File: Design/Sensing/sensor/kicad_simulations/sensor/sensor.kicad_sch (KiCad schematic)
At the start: 3 parts, among them J1 Conn_01x14_Pin, J2 Conn_01x14_Pin, J3 Conn_01x01_Pin

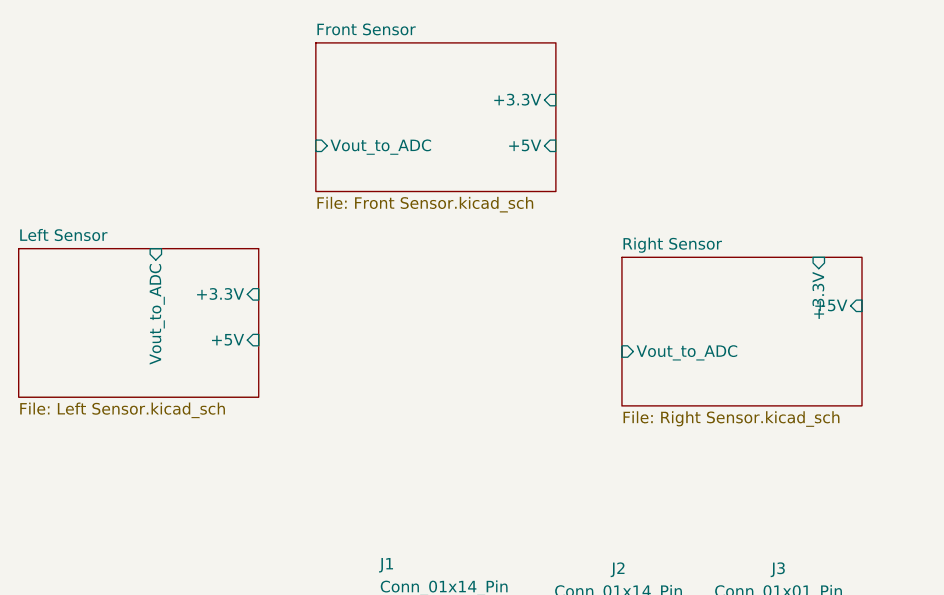
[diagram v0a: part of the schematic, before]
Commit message: Resistor values for emitter circuit done, still have to name the circuits properly
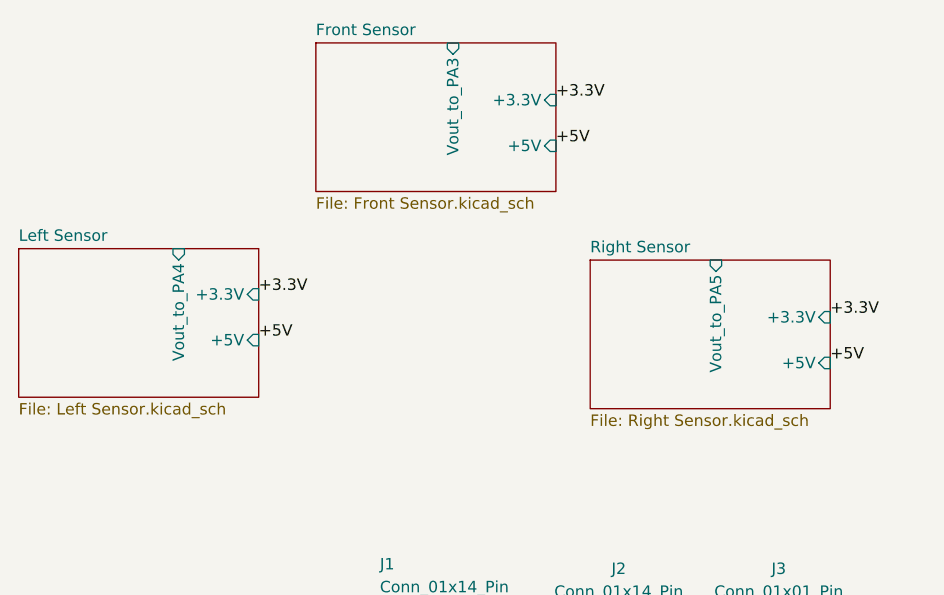
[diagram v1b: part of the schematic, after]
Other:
- sheet Front Sensor ports: added Vout_to_PA3; removed Vout_to_ADC
- sheet Left Sensor ports: added Vout_to_PA4; removed Vout_to_ADC
- sheet Right Sensor ports: added Vout_to_PA5; removed Vout_to_ADC
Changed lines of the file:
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@@
 	(generator_version "8.0")
 	(paper "A4")
+	(label "+5V"
+		(at 194.31 87.63 0)
+		(fields_autoplaced yes)
+		(effects
+			(font
+				(size 1.27 1.27)
+			)
+			(justify left bottom)
+		)
+	)
+	(label "+3.3V"
+		(at 194.31 82.55 0)
+		(fields_autoplaced yes)
+		(effects
+			(font
+				(size 1.27 1.27)
+			)
+			(justify left bottom)
+		)
+	)
+	(label "+5V"
+		(at 163.83 63.5 0)
+		(fields_autoplaced yes)
+		(effects
+			(font
+				(size 1.27 1.27)
+			)
+			(justify left bottom)
+		)
+	)
+	(label "+3.3V"
+		(at 163.83 58.42 0)
+		(fields_autoplaced yes)
+		(effects
+			(font
+				(size 1.27 1.27)
+			)
+			(justify left bottom)
+		)
+	)
+	(label "+3.3V"
+		(at 130.81 80.01 0)
+		(fields_autoplaced yes)
+		(effects
+			(font
+				(size 1.27 1.27)
+			)
+			(justify left bottom)
+		)
+	)
+	(label "+5V"
+		(at 130.81 85.09 0)
+		(fields_autoplaced yes)
+		(effects
+			(font
+				(size 1.27 1.27)
+			)
+			(justify left bottom)
+		)
+	)
 	(symbol
 		(lib_id "Connector:Conn_01x01_Pin")
@@
 			)
 		)
-		(pin "Vout_to_ADC" input
-			(at 137.16 63.5 180)
-			(effects
-				(font
-					(size 1.27 1.27)
-				)
-				(justify left)
-			)
-		)
 		(pin "+3.3V" input
 			(at 163.83 58.42 0)
@@
 		(pin "+5V" input
 			(at 163.83 63.5 0)
+			(effects
+				(font
+					(size 1.27 1.27)
+				)
+				(justify right)
+			)
+		)
+		(pin "Vout_to_PA3" input
+			(at 152.4 52.07 90)
 			(effects
 				(font
@@
 	)
 	(sheet
-		(at 171.1715 75.8907)
+		(at 167.64 76.2)
 		(size 26.67 16.51)
 		(fields_autoplaced yes)
@@
 		)
 		(property "Sheetname" "Right Sensor"
-			(at 171.1715 75.1791 0)
+			(at 167.64 75.4884 0)
 			(effects
 				(font
@@
 		)
 		(property "Sheetfile" "Right Sensor.kicad_sch"
-			(at 171.1715 92.9853 0)
+			(at 167.64 93.2946 0)
 			(effects
 				(font
@@
 			)
 		)
-		(pin "Vout_to_ADC" input
-			(at 171.1715 86.36 180)
-			(effects
-				(font
-					(size 1.27 1.27)
-				)
-				(justify left)
-			)
-		)
 		(pin "+3.3V" input
-			(at 193.04 75.8907 90)
+			(at 194.31 82.55 0)
 			(effects
 				(font
@@
 		)
 		(pin "+5V" input
-			(at 197.8415 81.28 0)
+			(at 194.31 87.63 0)
+			(effects
+				(font
+					(size 1.27 1.27)
+				)
+				(justify right)
+			)
+		)
+		(pin "Vout_to_PA5" input
+			(at 181.61 76.2 90)
 			(effects
 				(font
@@
 			)
 		)
-		(pin "Vout_to_ADC" input
-			(at 119.38 74.93 90)
-			(effects
-				(font
-					(size 1.27 1.27)
-				)
-				(justify right)
-			)
-		)
 		(pin "+3.3V" input
 			(at 130.81 80.01 0)
@@
 			(effects
 				(font
+					(size 1.27 1.27)
+				)
+				(justify right)
+			)
+		)
+		(pin "Vout_to_PA4" input
+			(at 121.92 74.93 90)
+			(effects
+				(font

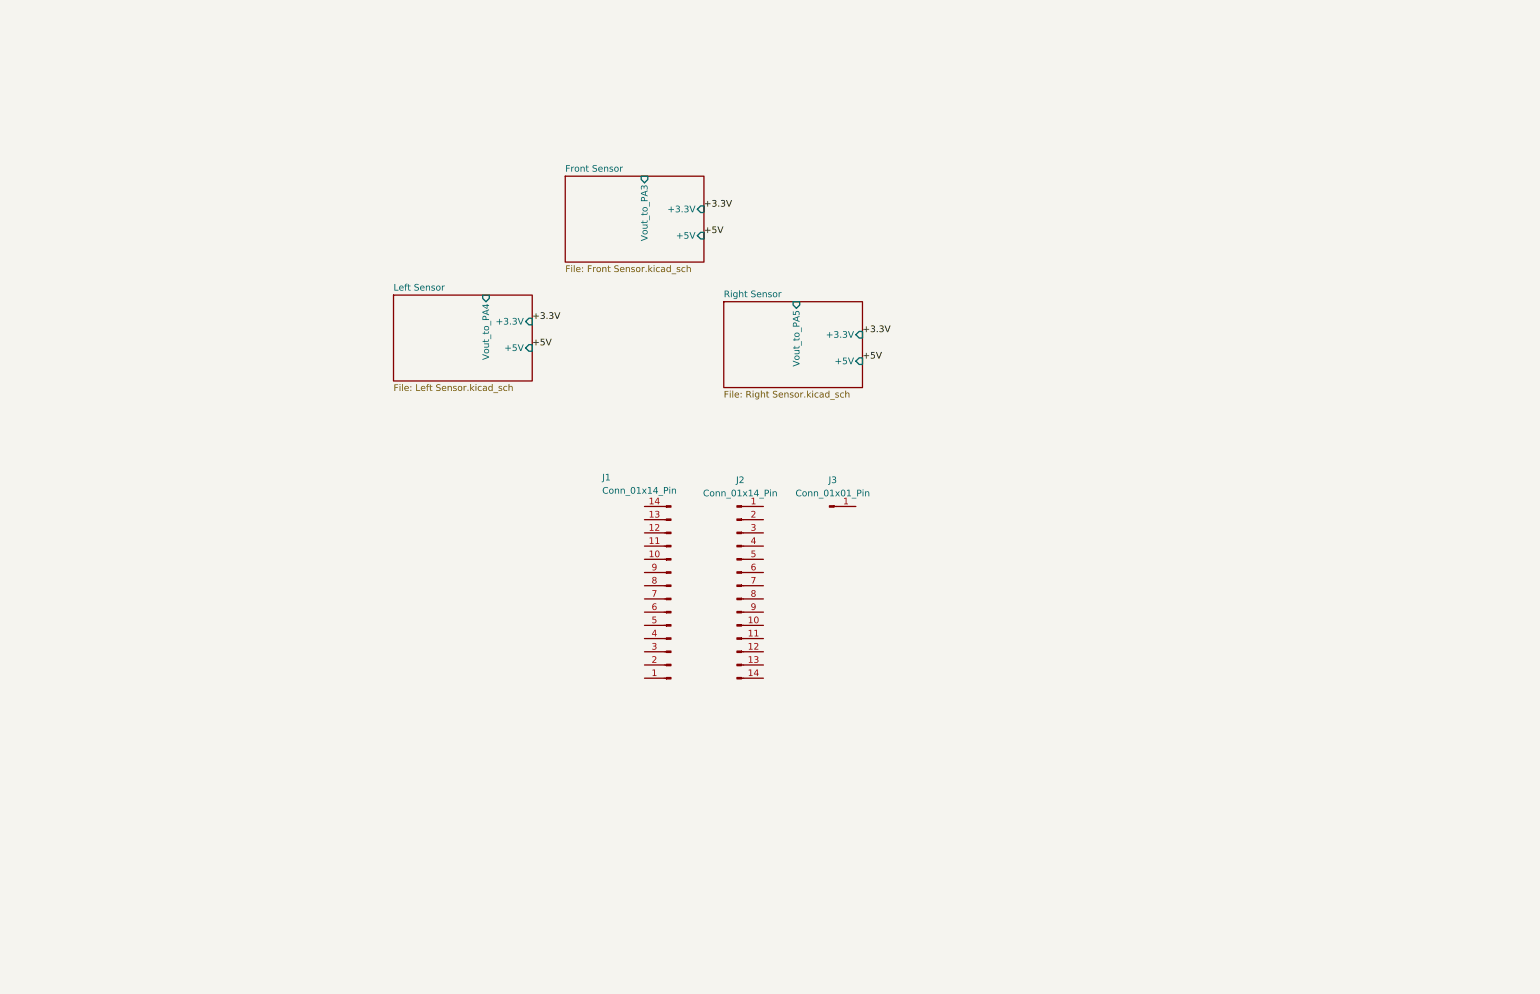
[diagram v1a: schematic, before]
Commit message: Sensing schematics done, the next stage is working on pcb component placement
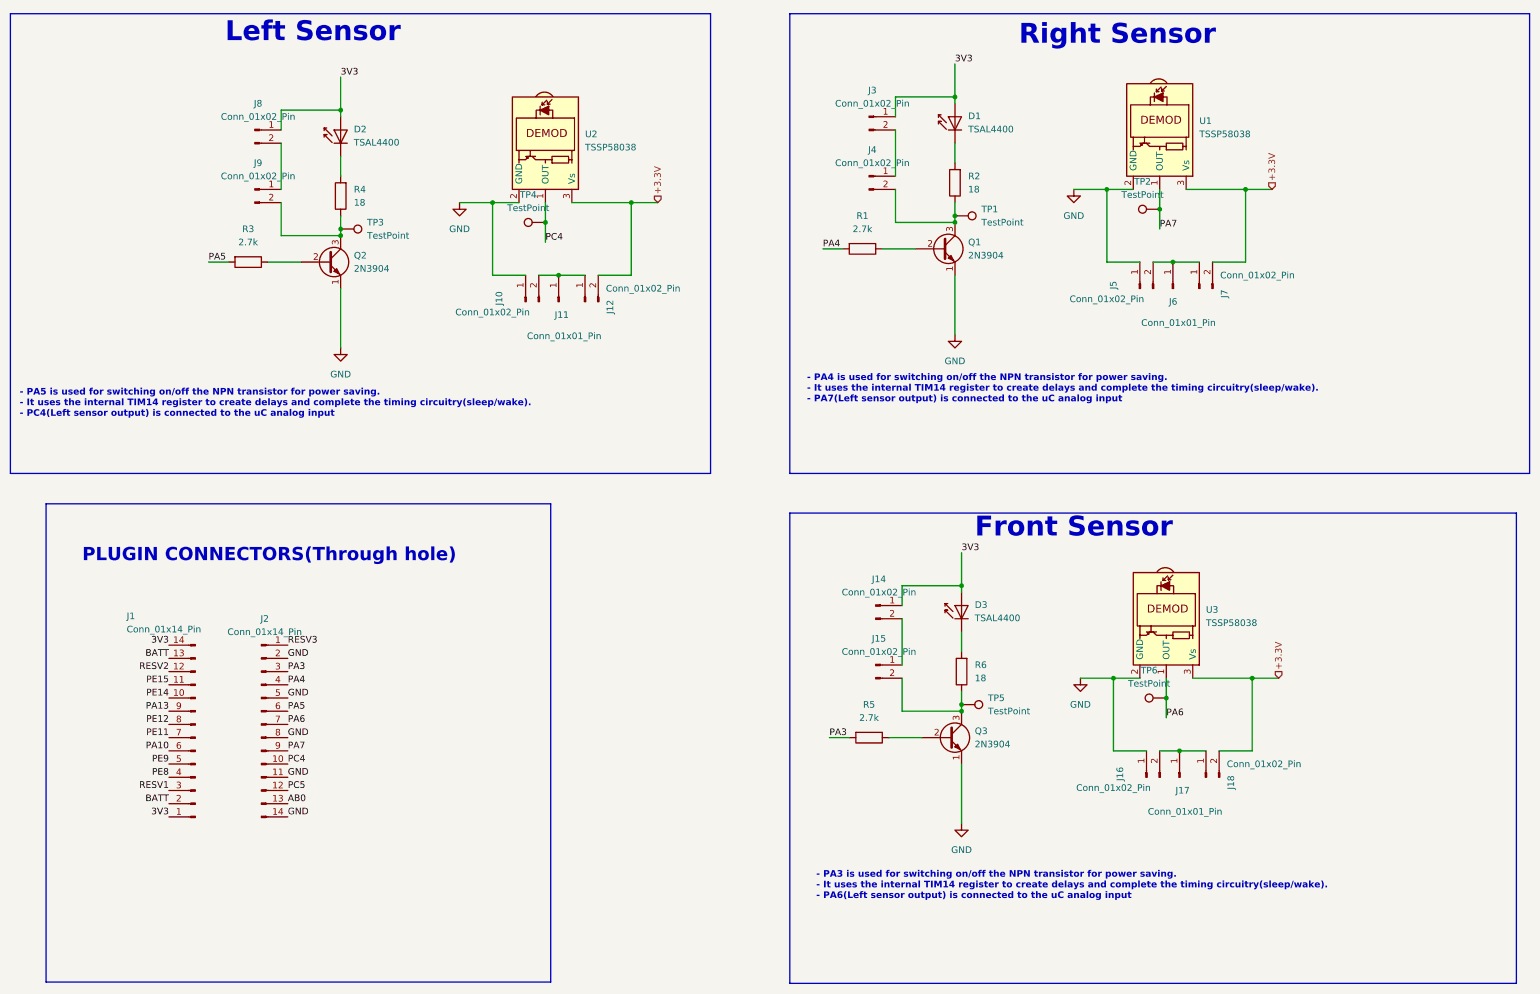
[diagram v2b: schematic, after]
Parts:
- removed J3: Conn_01x01_Pin, symbol Connector:Conn_01x01_Pin
- added D1, D2, D3: TSAL4400, LED_THT:LED_D3.0mm_IRBlack, symbol LED:TSAL4400
- added J10, J12, J14, J15, J16, J18, J3, J4, J5, J7, J8, J9: Conn_01x02_Pin, symbol Connector:Conn_01x02_Pin
- added J11, J17, J6: Conn_01x01_Pin, symbol Connector:Conn_01x01_Pin
- added Q1, Q2, Q3: 2N3904, Package_TO_SOT_THT:TO-92_Inline, symbol Transistor_BJT:2N3904
- added R1, R3, R5: 2.7k, symbol Device:R
- added R2, R4, R6: 18, symbol Device:R
- added TP1, TP2, TP3, TP4, TP5, TP6: TestPoint, symbol Connector:TestPoint
- added U1, U2, U3: TSSP58038, OptoDevice:Vishay_MINICAST-3Pin, symbol Sensor_Proximity:TSSP58038
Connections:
- net +3.3V: now also J12.2 (Pin_2), J18.2 (Pin_2), J7.2 (Pin_2), U1.3 (Vs), U2.3 (Vs), U3.3 (Vs)
- net 3V3: now reaches J1.1 (Pin_1)
- net 3V3: now also J1.14 (Pin_14), D1.2 (A), D2.2 (A), D3.2 (A), J14.1 (Pin_1), J3.1 (Pin_1), J8.1 (Pin_1)
- net PE14: now reaches J1.10 (Pin_10)
- net PE15: now reaches J1.11 (Pin_11)
- net RESV2: now reaches J1.12 (Pin_12)
- net BATT: now reaches J1.13 (Pin_13)
- net BATT: now also J1.2 (Pin_2)
- net RESV1: now reaches J1.3 (Pin_3)
- net PE8: now reaches J1.4 (Pin_4)
- net PE9: now reaches J1.5 (Pin_5)
- net PA10: now reaches J1.6 (Pin_6)
- net PE11: now reaches J1.7 (Pin_7)
- net PE12: now reaches J1.8 (Pin_8)
- net PA13: now reaches J1.9 (Pin_9)
- net RESV3: now reaches J2.1 (Pin_1)
- net PC4: now reaches J2.10 (Pin_10)
- net PC4: now also TP4.1, U2.1 (OUT)
- net GND: now reaches J2.11 (Pin_11)
- net GND: now also J2.14 (Pin_14), J2.2 (Pin_2), J2.5 (Pin_5), J2.8 (Pin_8), J10.1 (Pin_1), J16.1 (Pin_1), J5.1 (Pin_1), Q1.1 (E), Q2.1 (E), Q3.1 (E), U1.2 (GND), U2.2 (GND), U3.2 (GND)
- net PC5: now reaches J2.12 (Pin_12)
- net AB0: now reaches J2.13 (Pin_13)
- net PA3: now reaches J2.3 (Pin_3)
- net PA3: now also R5.2
- net PA4: now reaches J2.4 (Pin_4)
- net PA4: now also R1.2
- net PA5: now reaches J2.6 (Pin_6)
- net PA5: now also R3.2
- net PA6: now reaches J2.7 (Pin_7)
- net PA6: now also TP6.1, U3.1 (OUT)
- net PA7: now reaches J2.9 (Pin_9)
- net PA7: now also TP2.1, U1.1 (OUT)
- new net: J10.2 (Pin_2), J11.1 (Pin_1), J12.1 (Pin_1)
- new net: J5.2 (Pin_2), J6.1 (Pin_1), J7.1 (Pin_1)
- new net: J16.2 (Pin_2), J17.1 (Pin_1), J18.1 (Pin_1)
- new net: J3.2 (Pin_2), J4.1 (Pin_1)
- new net: J14.2 (Pin_2), J15.1 (Pin_1)
- new net: Q3.2 (B), R5.1
- new net: J15.2 (Pin_2), Q3.3 (C), R6.1, TP5.1
- new net: D2.1 (K), R4.2
- new net: J8.2 (Pin_2), J9.1 (Pin_1)
- new net: J9.2 (Pin_2), Q2.3 (C), R4.1, TP3.1
- new net: Q1.2 (B), R1.1
- new net: D3.1 (K), R6.2
- new net: J4.2 (Pin_2), Q1.3 (C), R2.1, TP1.1
- new net: D1.1 (K), R2.2
- new net: Q2.2 (B), R3.1
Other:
- removed sheet Front Sensor
- removed sheet Left Sensor
- removed sheet Right Sensor
- note added: "- PA3 is used for switching on/off the NPN transistor for power saving. - It uses the internal TIM14 register to create delays and complete the timing circuitry(sleep/wake). - PA6(Left sensor output) is connected to the uC analog input"
- note added: "- PA4 is used for switching on/off the NPN transistor for power saving. - It uses the internal TIM14 register to create delays and complete the timing circuitry(sleep/wake). - PA7(Left sensor output) is connected to the uC analog input"
- note added: "- PA5 is used for switching on/off the NPN transistor for power saving. - It uses the internal TIM14 register to create delays and complete the timing circuitry(sleep/wake). - PC4(Left sensor output) is connected to the uC analog input"
- note added: "Front Sensor"
- note added: "Left Sensor"
- note added: "PLUGIN CONNECTORS(Through hole)"
- note added: "Right Sensor"
- moved on the sheet: J1, J2

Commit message: Footprints assigned
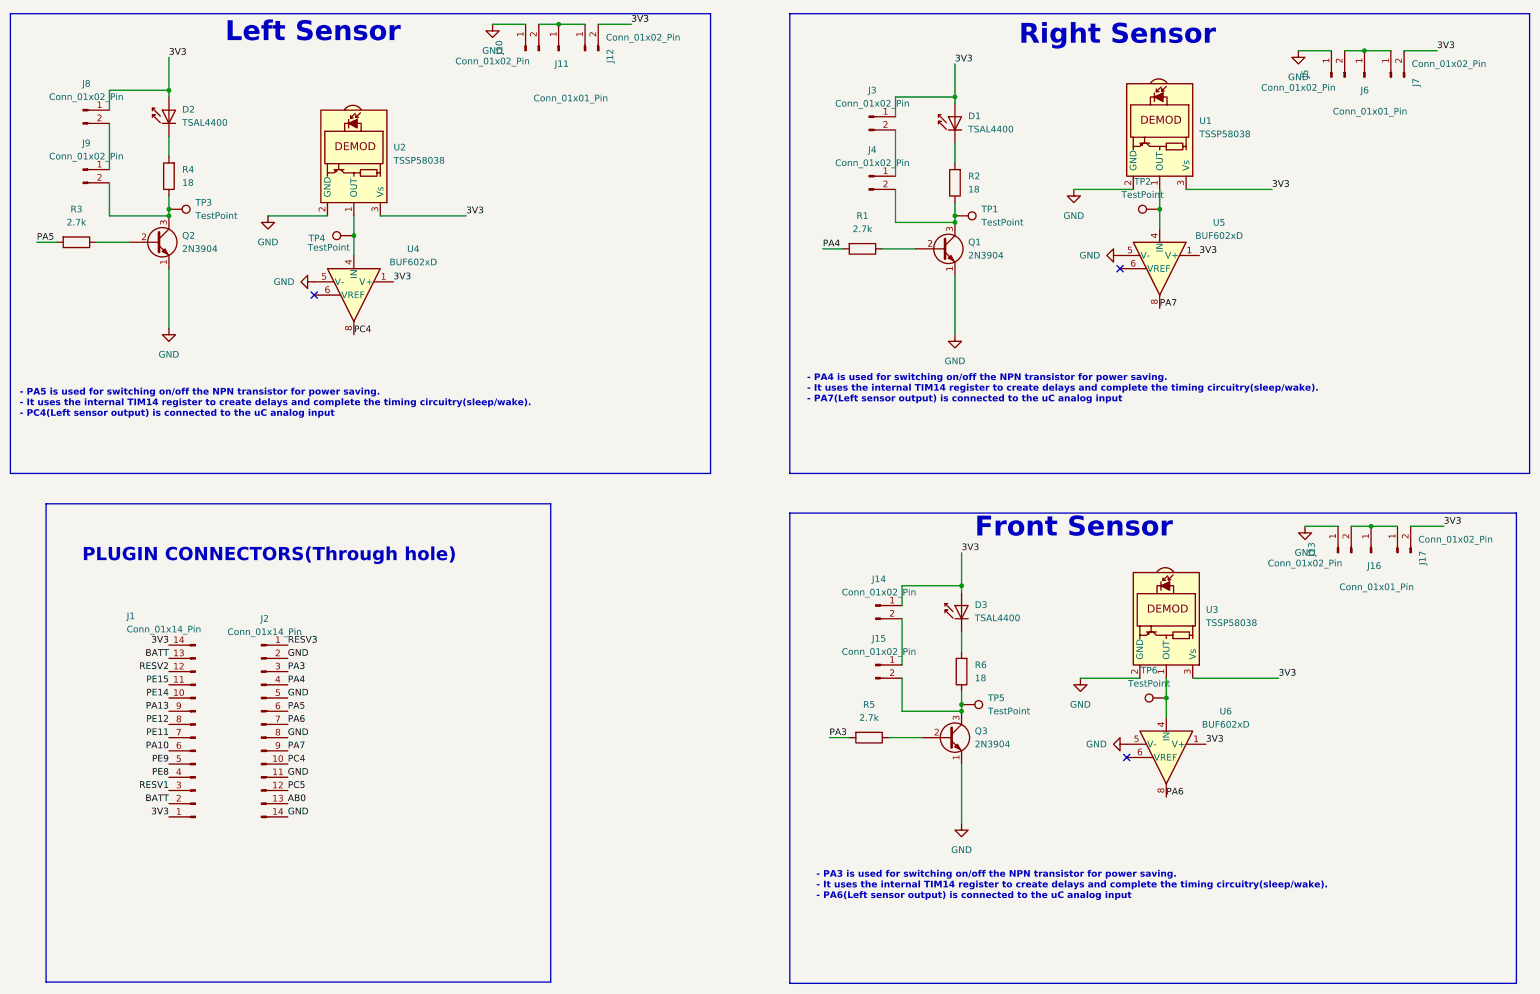
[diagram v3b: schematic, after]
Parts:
- removed J16, J18: Conn_01x02_Pin, symbol Connector:Conn_01x02_Pin
- removed J17: Conn_01x01_Pin, symbol Connector:Conn_01x01_Pin
- added J13, J17: Conn_01x02_Pin, Connector_PinHeader_2.54mm:PinHeader_1x02_P2.54mm_Vertical, symbol Connector:Conn_01x02_Pin
- added J16: Conn_01x01_Pin, Connector_PinHeader_2.54mm:PinHeader_1x01_P2.54mm_Vertical, symbol Connector:Conn_01x01_Pin
- added U4, U5, U6: BUF602xD, Package_SO:SOIC-8_3.9x4.9mm_P1.27mm, symbol Amplifier_Buffer:BUF602xD
- J1, J2: footprint (none) -> Connector_PinHeader_2.54mm:PinHeader_1x14_P2.54mm_Vertical
- J10, J12, J14, J15, J3, J4, J5, J7, J8, J9: footprint (none) -> Connector_PinHeader_2.54mm:PinHeader_1x02_P2.54mm_Vertical
- J11, J6: footprint (none) -> Connector_PinHeader_2.54mm:PinHeader_1x01_P2.54mm_Vertical
- R1, R2, R3, R4, R5, R6: footprint (none) -> Resistor_SMD:R_1206_3216Metric
- TP1, TP2, TP3, TP4, TP5, TP6: footprint (none) -> TestPoint:TestPoint_2Pads_Pitch2.54mm_Drill0.8mm
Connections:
- net +3.3V is gone; now on net 3V3: J12.2 (Pin_2), J7.2 (Pin_2), U1.3 (Vs), U2.3 (Vs), U3.3 (Vs)
- net 3V3: now also J17.2 (Pin_2), U4.1 (V+), U5.1 (V+), U6.1 (V+)
- net GND: now also J13.1 (Pin_1), U4.5 (V-), U5.5 (V-), U6.5 (V-)
- net PA6: now also U6.8; no longer TP6.1, U3.1 (OUT)
- net PA7: now also U5.8; no longer TP2.1, U1.1 (OUT)
- net PC4: now also U4.8; no longer TP4.1, U2.1 (OUT)
- new net: TP6.1, U3.1 (OUT), U6.4 (IN)
- new net: TP4.1, U2.1 (OUT), U4.4 (IN)
- new net: J13.2 (Pin_2), J16.1 (Pin_1), J17.1 (Pin_1)
- new net: TP2.1, U1.1 (OUT), U5.4 (IN)
- no-connect marks 0 -> 3
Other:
- moved on the sheet: D2, J5, J6, J7, J8, J9, Q2, R3, R4, TP3, TP4, U2
